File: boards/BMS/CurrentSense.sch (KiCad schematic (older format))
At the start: 8 parts

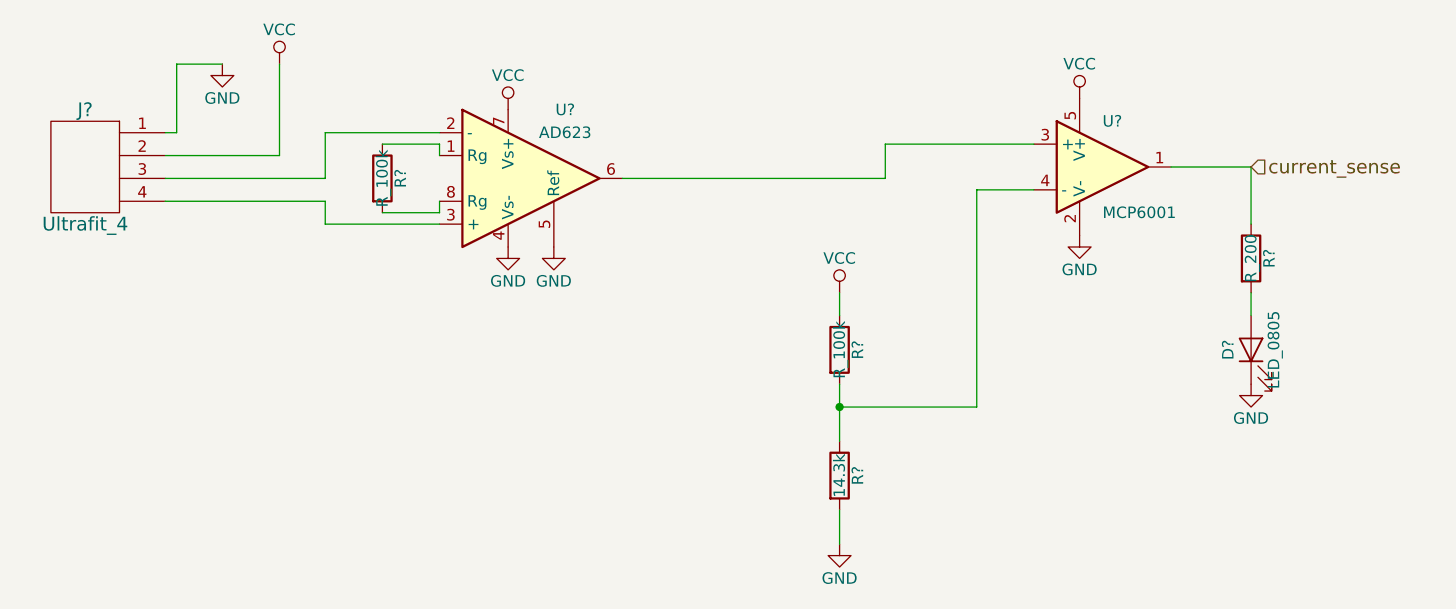
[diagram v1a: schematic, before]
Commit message: edited discharge circuit schematic
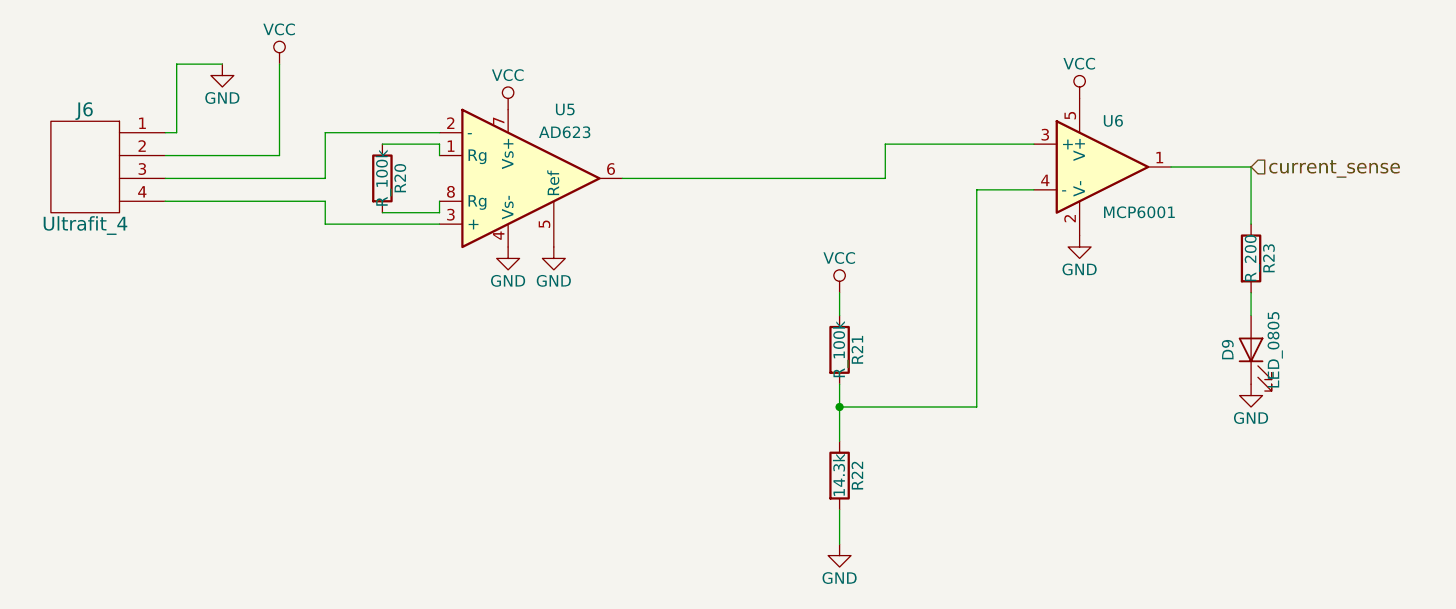
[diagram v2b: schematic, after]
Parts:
- gave numbers to parts that had none: 8
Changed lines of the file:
@@
 $EndDescr
 $Comp
-L MCP6001 U?
+L MCP6001 U6
 U 1 1 59E289F1
 P 7050 3450
-F 0 "U?" H 7050 3650 50  0000 L CNN
+F 0 "U6" H 7050 3650 50  0000 L CNN
 F 1 "MCP6001" H 7050 3250 50  0000 L CNN
 F 2 "" H 7050 3450 50  0001 C CNN
@@
 $EndComp
 $Comp
-L Ultrafit_4 J?
+L Ultrafit_4 J6
 U 1 1 59E29101
 P 2600 3500
-F 0 "J?" H 2600 3800 60  0000 C CNN
+F 0 "J6" H 2600 3800 60  0000 C CNN
 F 1 "Ultrafit_4" H 2600 3300 60  0000 C CNN
 F 2 "footprints:Ultrafit_4" H 2500 3750 60  0001 C CNN
@@
 $EndComp
 $Comp
-L GND #PWR?
+L GND #PWR042
 U 1 1 59E292C4
 P 3200 3000
-F 0 "#PWR?" H 3200 2750 50  0001 C CNN
+F 0 "#PWR042" H 3200 2750 50  0001 C CNN
 F 1 "GND" H 3200 2850 50  0000 C CNN
 F 2 "" H 3200 3000 50  0001 C CNN
@@
 $EndComp
 $Comp
-L VCC #PWR?
+L VCC #PWR043
 U 1 1 59E292DC
 P 3450 3000
-F 0 "#PWR?" H 3450 2850 50  0001 C CNN
+F 0 "#PWR043" H 3450 2850 50  0001 C CNN
 F 1 "VCC" H 3450 3150 50  0000 C CNN
 F 2 "" H 3450 3000 50  0001 C CNN
@@
 	3450 3400 3450 3000
 $Comp
-L AD623 U?
+L AD623 U5
 U 1 1 59E29301
 P 4550 3500
-F 0 "U?" H 4700 3800 50  0000 C CNN
+F 0 "U5" H 4700 3800 50  0000 C CNN
 F 1 "AD623" H 4700 3700 50  0000 C CNN
 F 2 "" H 4550 3500 50  0001 C CNN
@@
 	3650 3700 4150 3700
 $Comp
-L GND #PWR?
+L GND #PWR044
 U 1 1 59E2937F
 P 4450 3800
-F 0 "#PWR?" H 4450 3550 50  0001 C CNN
+F 0 "#PWR044" H 4450 3550 50  0001 C CNN
 F 1 "GND" H 4450 3650 50  0000 C CNN
 F 2 "" H 4450 3800 50  0001 C CNN
@@
 $EndComp
 $Comp
-L VCC #PWR?
+L VCC #PWR045
 U 1 1 59E29399
 P 4450 3200
-F 0 "#PWR?" H 4450 3050 50  0001 C CNN
+F 0 "#PWR045" H 4450 3050 50  0001 C CNN
 F 1 "VCC" H 4450 3350 50  0000 C CNN
 F 2 "" H 4450 3200 50  0001 C CNN
@@
 $EndComp
 $Comp
-L GND #PWR?
+L GND #PWR046
 U 1 1 59E293B3
 P 4650 3800
-F 0 "#PWR?" H 4650 3550 50  0001 C CNN
+F 0 "#PWR046" H 4650 3550 50  0001 C CNN
 F 1 "GND" H 4650 3650 50  0000 C CNN
 F 2 "" H 4650 3800 50  0001 C CNN
@@
 $EndComp
 $Comp
-L R_100k R?
+L R_100k R20
 U 1 1 59E293CD
 P 3900 3500
-F 0 "R?" V 3980 3500 50  0000 C CNN
+F 0 "R20" V 3980 3500 50  0000 C CNN
 F 1 "R_100k" V 3900 3500 50  0000 C CNN
 F 2 "Resistors_SMD:R_0805" H 3830 3500 50  0001 C CNN
@@
 	6100 3350 6750 3350
 $Comp
-L GND #PWR?
+L GND #PWR047
 U 1 1 59E2948A
 P 6950 3750
-F 0 "#PWR?" H 6950 3500 50  0001 C CNN
+F 0 "#PWR047" H 6950 3500 50  0001 C CNN
 F 1 "GND" H 6950 3600 50  0000 C CNN
 F 2 "" H 6950 3750 50  0001 C CNN
@@
 $EndComp
 $Comp
-L VCC #PWR?
+L VCC #PWR048
 U 1 1 59E294A6
 P 6950 3150
-F 0 "#PWR?" H 6950 3000 50  0001 C CNN
+F 0 "#PWR048" H 6950 3000 50  0001 C CNN
 F 1 "VCC" H 6950 3300 50  0000 C CNN
 F 2 "" H 6950 3150 50  0001 C CNN
@@
 $EndComp
 $Comp
-L VCC #PWR?
+L VCC #PWR049
 U 1 1 59E294C8
 P 5900 4000
-F 0 "#PWR?" H 5900 3850 50  0001 C CNN
+F 0 "#PWR049" H 5900 3850 50  0001 C CNN
 F 1 "VCC" H 5900 4150 50  0000 C CNN
 F 2 "" H 5900 4000 50  0001 C CNN
@@
 $EndComp
 $Comp
-L R_100k R?
+L R_100k R21
 U 1 1 59E294E4
 P 5900 4250
-F 0 "R?" V 5980 4250 50  0000 C CNN
+F 0 "R21" V 5980 4250 50  0000 C CNN
 F 1 "R_100k" V 5900 4250 50  0000 C CNN
 F 2 "Resistors_SMD:R_0805" H 5830 4250 50  0001 C CNN
@@
 $EndComp
 $Comp
-L R R?
+L R R22
 U 1 1 59E29525
 P 5900 4800
-F 0 "R?" V 5980 4800 50  0000 C CNN
+F 0 "R22" V 5980 4800 50  0000 C CNN
 F 1 "14.3k" V 5900 4800 50  0000 C CNN
 F 2 "" V 5830 4800 50  0001 C CNN
@@
 $EndComp
 $Comp
-L GND #PWR?
+L GND #PWR050
 U 1 1 59E2956B
 P 5900 5100
-F 0 "#PWR?" H 5900 4850 50  0001 C CNN
+F 0 "#PWR050" H 5900 4850 50  0001 C CNN
 F 1 "GND" H 5900 4950 50  0000 C CNN
 F 2 "" H 5900 5100 50  0001 C CNN
@@
 Connection ~ 5900 4500
 $Comp
-L R_200 R?
+L R_200 R23
 U 1 1 59E29633
 P 7700 3850
-F 0 "R?" V 7780 3850 50  0000 C CNN
+F 0 "R23" V 7780 3850 50  0000 C CNN
 F 1 "R_200" V 7700 3850 50  0000 C CNN
 F 2 "Resistors_SMD:R_0805" H 7630 3850 50  0001 C CNN
@@
 $EndComp
 $Comp
-L LED_0805 D?
+L LED_0805 D9
 U 1 1 59E2967C
 P 7700 4250
-F 0 "D?" H 7700 4350 50  0000 C CNN
+F 0 "D9" H 7700 4350 50  0000 C CNN
 F 1 "LED_0805" H 7700 4150 50  0000 C CNN
 F 2 "LEDs:LED_0805" H 7600 4250 50  0001 C CNN
@@
 	7700 4000 7700 4100
 $Comp
-L GND #PWR?
+L GND #PWR051
 U 1 1 59E29733
 P 7700 4400
-F 0 "#PWR?" H 7700 4150 50  0001 C CNN
+F 0 "#PWR051" H 7700 4150 50  0001 C CNN
 F 1 "GND" H 7700 4250 50  0000 C CNN
 F 2 "" H 7700 4400 50  0001 C CNN

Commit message: Progress
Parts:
- D9: footprint LEDs:LED_0805 -> footprints:LED_0805_OEM
- R20, R21, R23: footprint Resistors_SMD:R_0805 -> footprints:R_0805_OEM
- R22: footprint (none) -> footprints:R_0805_OEM
- U5: footprint (none) -> footprints:AD623_SOIC-8
- U6: footprint (none) -> footprints:SOT-23-5_OEM
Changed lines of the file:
@@
 F 0 "U6" H 7050 3650 50  0000 L CNN
 F 1 "MCP6001" H 7050 3250 50  0000 L CNN
-F 2 "" H 7050 3450 50  0001 C CNN
+F 2 "footprints:SOT-23-5_OEM" H 7050 3450 50  0001 C CNN
 F 3 "" H 7050 3650 50  0001 C CNN
 	1    7050 3450
@@
 $EndComp
 $Comp
-L GND #PWR039
+L GND #PWR034
 U 1 1 59E292C4
 P 3200 3000
-F 0 "#PWR039" H 3200 2750 50  0001 C CNN
+F 0 "#PWR034" H 3200 2750 50  0001 C CNN
 F 1 "GND" H 3200 2850 50  0000 C CNN
 F 2 "" H 3200 3000 50  0001 C CNN
@@
 $EndComp
 $Comp
-L VCC #PWR040
+L VCC #PWR035
 U 1 1 59E292DC
 P 3450 3000
-F 0 "#PWR040" H 3450 2850 50  0001 C CNN
+F 0 "#PWR035" H 3450 2850 50  0001 C CNN
 F 1 "VCC" H 3450 3150 50  0000 C CNN
 F 2 "" H 3450 3000 50  0001 C CNN
@@
 Wire Wire Line
 	3450 3400 3450 3000
-$Comp
-L AD623 U5
-U 1 1 59E29301
-P 4550 3500
-F 0 "U5" H 4700 3800 50  0000 C CNN
-F 1 "AD623" H 4700 3700 50  0000 C CNN
-F 2 "" H 4550 3500 50  0001 C CNN
-F 3 "" H 4550 3500 50  0001 C CNN
-	1    4550 3500
-	1    0    0    -1
-$EndComp
 Wire Wire Line
 	4150 3300 3650 3300
@@
 	3650 3700 4150 3700
 $Comp
-L GND #PWR041
+L GND #PWR036
 U 1 1 59E2937F
 P 4450 3800
-F 0 "#PWR041" H 4450 3550 50  0001 C CNN
+F 0 "#PWR036" H 4450 3550 50  0001 C CNN
 F 1 "GND" H 4450 3650 50  0000 C CNN
 F 2 "" H 4450 3800 50  0001 C CNN
@@
 $EndComp
 $Comp
-L VCC #PWR042
+L VCC #PWR037
 U 1 1 59E29399
 P 4450 3200
-F 0 "#PWR042" H 4450 3050 50  0001 C CNN
+F 0 "#PWR037" H 4450 3050 50  0001 C CNN
 F 1 "VCC" H 4450 3350 50  0000 C CNN
 F 2 "" H 4450 3200 50  0001 C CNN
@@
 $EndComp
 $Comp
-L GND #PWR043
+L GND #PWR038
 U 1 1 59E293B3
 P 4650 3800
-F 0 "#PWR043" H 4650 3550 50  0001 C CNN
+F 0 "#PWR038" H 4650 3550 50  0001 C CNN
 F 1 "GND" H 4650 3650 50  0000 C CNN
 F 2 "" H 4650 3800 50  0001 C CNN
@@
 F 0 "R20" V 3980 3500 50  0000 C CNN
 F 1 "R_100k" V 3900 3500 50  0000 C CNN
-F 2 "Resistors_SMD:R_0805" H 3830 3500 50  0001 C CNN
+F 2 "footprints:R_0805_OEM" H 3830 3500 50  0001 C CNN
 F 3 "http://www.yageo.com.tw/exep/pages/download/literatures/PYu-R_INT-thick_7.pdf" H 3980 3500 50  0001 C CNN
 F 4 "311-100KCRCT-ND" H 3900 3500 60  0001 C CNN "MPN"
@@
 	6100 3350 6750 3350
 $Comp
-L GND #PWR044
+L GND #PWR039
 U 1 1 59E2948A
 P 6950 3750
-F 0 "#PWR044" H 6950 3500 50  0001 C CNN
+F 0 "#PWR039" H 6950 3500 50  0001 C CNN
 F 1 "GND" H 6950 3600 50  0000 C CNN
 F 2 "" H 6950 3750 50  0001 C CNN
@@
 $EndComp
 $Comp
-L VCC #PWR045
+L VCC #PWR040
 U 1 1 59E294A6
 P 6950 3150
-F 0 "#PWR045" H 6950 3000 50  0001 C CNN
+F 0 "#PWR040" H 6950 3000 50  0001 C CNN
 F 1 "VCC" H 6950 3300 50  0000 C CNN
 F 2 "" H 6950 3150 50  0001 C CNN
@@
 $EndComp
 $Comp
-L VCC #PWR046
+L VCC #PWR041
 U 1 1 59E294C8
 P 5900 4000
-F 0 "#PWR046" H 5900 3850 50  0001 C CNN
+F 0 "#PWR041" H 5900 3850 50  0001 C CNN
 F 1 "VCC" H 5900 4150 50  0000 C CNN
 F 2 "" H 5900 4000 50  0001 C CNN
@@
 F 0 "R21" V 5980 4250 50  0000 C CNN
 F 1 "R_100k" V 5900 4250 50  0000 C CNN
-F 2 "Resistors_SMD:R_0805" H 5830 4250 50  0001 C CNN
+F 2 "footprints:R_0805_OEM" H 5830 4250 50  0001 C CNN
 F 3 "http://www.yageo.com.tw/exep/pages/download/literatures/PYu-R_INT-thick_7.pdf" H 5980 4250 50  0001 C CNN
 F 4 "311-100KCRCT-ND" H 5900 4250 60  0001 C CNN "MPN"
@@
 F 0 "R22" V 5980 4800 50  0000 C CNN
 F 1 "14.3k" V 5900 4800 50  0000 C CNN
-F 2 "" V 5830 4800 50  0001 C CNN
+F 2 "footprints:R_0805_OEM" V 5830 4800 50  0001 C CNN
 F 3 "" H 5900 4800 50  0001 C CNN
 	1    5900 4800
@@
 $EndComp
 $Comp
-L GND #PWR047
+L GND #PWR042
 U 1 1 59E2956B
 P 5900 5100
-F 0 "#PWR047" H 5900 4850 50  0001 C CNN
+F 0 "#PWR042" H 5900 4850 50  0001 C CNN
 F 1 "GND" H 5900 4950 50  0000 C CNN
 F 2 "" H 5900 5100 50  0001 C CNN
@@
 F 0 "R23" V 7780 3850 50  0000 C CNN
 F 1 "R_200" V 7700 3850 50  0000 C CNN
-F 2 "Resistors_SMD:R_0805" H 7630 3850 50  0001 C CNN
+F 2 "footprints:R_0805_OEM" H 7630 3850 50  0001 C CNN
 F 3 "https://www.seielect.com/Catalog/SEI-RMCF_RMCP.pdf" H 7780 3850 50  0001 C CNN
 F 4 "Digi-Key" H 7700 3850 60  0001 C CNN "MFN"
@@
 F 0 "D9" H 7700 4350 50  0000 C CNN
 F 1 "LED_0805" H 7700 4150 50  0000 C CNN
-F 2 "LEDs:LED_0805" H 7600 4250 50  0001 C CNN
+F 2 "footprints:LED_0805_OEM" H 7600 4250 50  0001 C CNN
 F 3 "http://www.osram-os.com/Graphics/XPic9/00078860_0.pdf" H 7700 4350 50  0001 C CNN
 F 4 "475-1410-1-ND" H 7700 4250 60  0001 C CNN "MPN"
@@
 	7700 4000 7700 4100
 $Comp
-L GND #PWR048
+L GND #PWR043
 U 1 1 59E29733
 P 7700 4400
-F 0 "#PWR048" H 7700 4150 50  0001 C CNN
+F 0 "#PWR043" H 7700 4150 50  0001 C CNN
 F 1 "GND" H 7700 4250 50  0000 C CNN
 F 2 "" H 7700 4400 50  0001 C CNN
@@
 Text HLabel 7700 3450 2    60   Input ~ 0
 current_sense
+$Comp
+L AD623 U5
+U 1 1 5A1D356C
+P 4550 3500
+F 0 "U5" H 4700 3800 50  0000 C CNN
+F 1 "AD623" H 4700 3700 50  0000 C CNN
+F 2 "footprints:AD623_SOIC-8" H 4550 3500 50  0001 C CNN
+F 3 "" H 4550 3500 50  0001 C CNN
+	1    4550 3500
+	1    0    0    -1
+$EndComp
 $EndSCHEMATC
